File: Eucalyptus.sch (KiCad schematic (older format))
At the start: 39 parts

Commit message: modificaciones
se empezo el sch y pcb
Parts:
- removed C? (x2): 10uF, EESTN5:CAP_ELEC_5x11mm, symbol Eucalyptus-rescue:CAPAPOL-2018---MiniSumo---NANO---DRV8872-rescue
- removed J?: Sensor TATAMI FI, EESTN5:Pin_Strip_3, symbol Eucalyptus-rescue:CONN_01X03-2018---MiniSumo---NANO---DRV8872-rescue
- removed J?: Sensor TATAMI TD, EESTN5:Pin_Strip_3, symbol Eucalyptus-rescue:CONN_01X03-2018---MiniSumo---NANO---DRV8872-rescue
- removed J?: Sensor TATAMI FD, EESTN5:Pin_Strip_3, symbol Eucalyptus-rescue:CONN_01X03-2018---MiniSumo---NANO---DRV8872-rescue
- removed J?: Bateria, EESTN5:BORNERA2_AZUL, symbol Eucalyptus-rescue:TB_1X2-2018---MiniSumo---NANO---DRV8872-rescue
- removed J?: Frontal Izquierdo, EESTN5:Pin_Strip_3, symbol Eucalyptus-rescue:CONN_01X03-2018---MiniSumo---NANO---DRV8872-rescue
- removed J?: Izquierdo, EESTN5:Pin_Strip_3, symbol Eucalyptus-rescue:CONN_01X03-2018---MiniSumo---NANO---DRV8872-rescue
- removed J?: Derecho, EESTN5:Pin_Strip_3, symbol Eucalyptus-rescue:CONN_01X03-2018---MiniSumo---NANO---DRV8872-rescue
- removed J?: Frontal Derecho, EESTN5:Pin_Strip_3, symbol Eucalyptus-rescue:CONN_01X03-2018---MiniSumo---NANO---DRV8872-rescue
- added C12, C14: C, EESTN5:C_1206, symbol EESTN5:C
- added C13, C15: CAPAPOL, EESTN5:CAP_ELEC_SMD_4X5.5, symbol EESTN5:CAPAPOL
- added Display1: SSD1306-SSD1306-128x64_OLED, EESTN5:128x64OLED, symbol EESTN5:SSD1306-SSD1306-128x64_OLED
- added H1, H2, H3, H4: Mounting_Hole, EESTN5:Separador_M3_5mm, symbol EESTN5:Mounting_Hole
- added J1, J16, J17: HEADER_2, Connector_JST:JST_EH_B2B-EH-A_1x02_P2.50mm_Vertical, symbol EESTN5:HEADER_2
- added J11, J12, J13, J14, J15, J3, J4, J5, J6, J7, J8, J9: HEADER_1, EESTN5:PAD_SMD_2x5mm, symbol EESTN5:HEADER_1
- added R10, R9: R, EESTN5:R_1206, symbol EESTN5:R
- added R11, R12: 0,,25, EESTN5:R_1206, symbol EESTN5:R
- added U3, U4: DRV8872, EESTN5:SSOP-8, symbol EESTN5:DRV8872
- C1, C10, C4: renamed from C?; footprint EESTN5:CAP_ELEC_5x11mm -> EESTN5:CAP_ELEC_SMD_4X5.5
- R4, R5: renamed from R?; footprint EESTN5:RES0.3 -> EESTN5:R_1206
- SW1: renamed from SW?; footprint EESTN5:Pulsador_TH_4 -> Button_Switch_SMD:SW_SPST_TL3342
- Y1: renamed from Y?; footprint EESTN5:HC49_SMD -> EESTN5:C_1206
- gave numbers to parts that had none: 22
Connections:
- net +5V: now also Display1.2 (VCC), J11.1, J14.1, J4.1, J7.1, R10.1, R9.1
- net DISTANCIA_D: now also J8.1
- net DISTANCIA_FD: now also J12.1
- net DISTANCIA_FI: now also J15.1
- net DISTANCIA_I: now also J5.1
- net GND: now also C12.2, C13.2, C14.2, C15.2, Display1.1 (GND), J1.1, J13.1, J3.1, J6.1, J9.1, R11.2, R12.2, U3.1 (GND), U4.1 (GND)
- net M1A: now also U3.2 (IN2)
- net M1B: now also U3.3 (IN1)
- net M2A: now also U4.2 (IN2)
- net M2B: now also U4.3 (IN1)
- net Vin: now also C12.1, C13.1, C14.1, C15.1, J1.2, U3.5 (VM), U4.5 (VM)
- net TATAMI_FD renamed SDA
- net SDA: now also Display1.4 (SDA), R10.2
- net TATAMI_FI renamed SCL
- net SCL: now also Display1.3 (SCL), R9.2
- new net: R11.1, U3.7 (ISEN)
- new net: J16.2, U3.6 (OUT1)
- new net: J16.1, U3.8 (OUT2)
- new net: J17.2, U4.6 (OUT1)
- new net: R12.1, U4.7 (ISEN)
- new net: J17.1, U4.8 (OUT2)
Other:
- moved on the sheet: BZ1, C1, C10, C11, C3, C4, C6, C7, C8, C9, D1, D2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

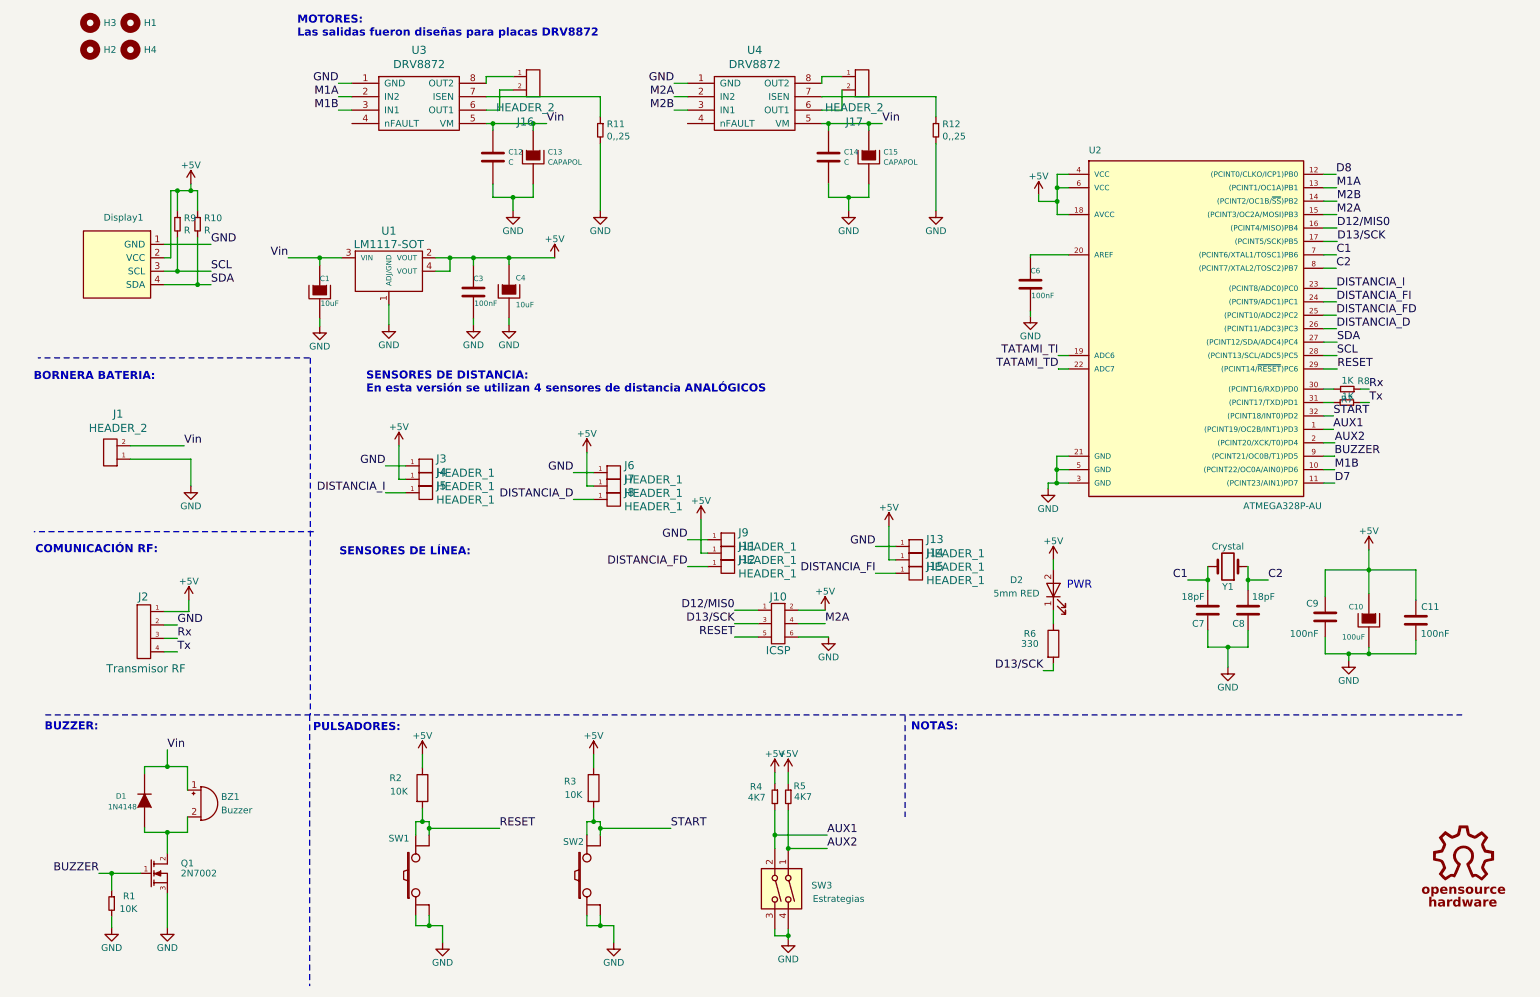
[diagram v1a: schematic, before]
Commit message: modificaciones
se agrego pdf de sch
pdf de lista de componentes y excel
tambien se modifico sch y pcb
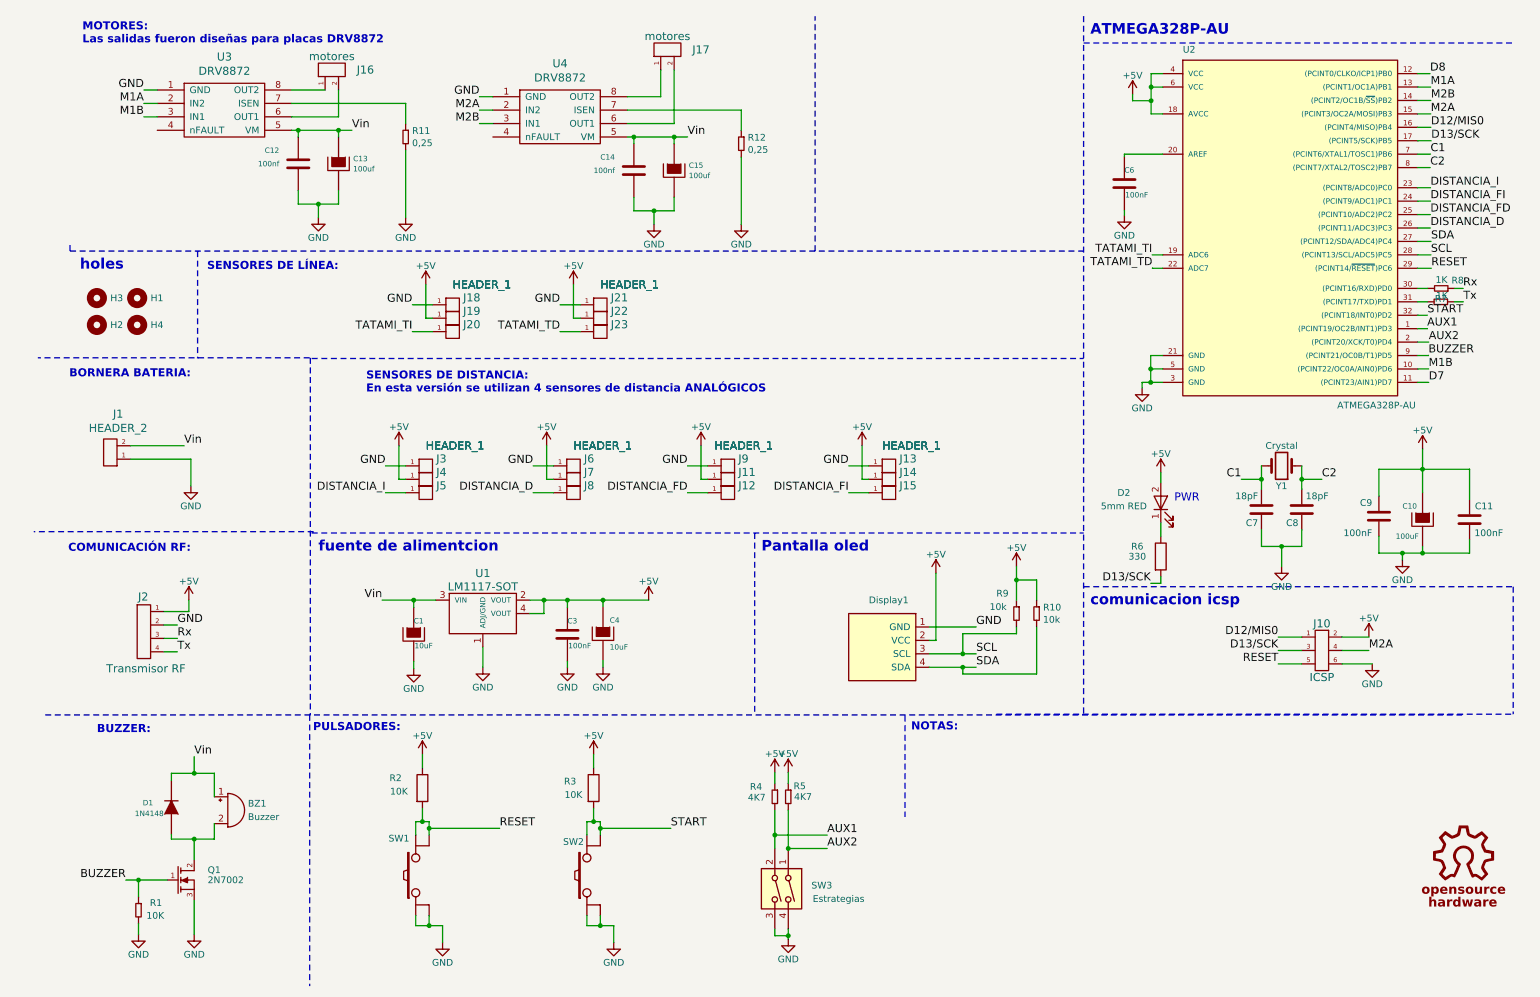
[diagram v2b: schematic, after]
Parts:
- added J18, J19, J20, J21, J22, J23: HEADER_1, EESTN5:PAD_SMD_2x5mm, symbol EESTN5:HEADER_1
- C12, C14: value C -> 100nf
- C13, C15: value CAPAPOL -> 100uf
- J16, J17: value HEADER_2 -> motores
- R10, R9: value R -> 10k
- R11, R12: value 0,,25 -> 0,25
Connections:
- net +5V: now also J19.1, J22.1
- net GND: now also J18.1, J21.1
- net TATAMI_TD: now also J23.1
- net TATAMI_TI: now also J20.1
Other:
- note added: "ATMEGA328P-AU"
- note added: "\nPantalla oled\n"
- note added: "comunicacion icsp"
- note added: "fuente de alimentcion"
- note added: "holes"
- moved on the sheet: BZ1, C1, C10, C11, C12, C13, C14, C15, C3, C4, C6, C7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

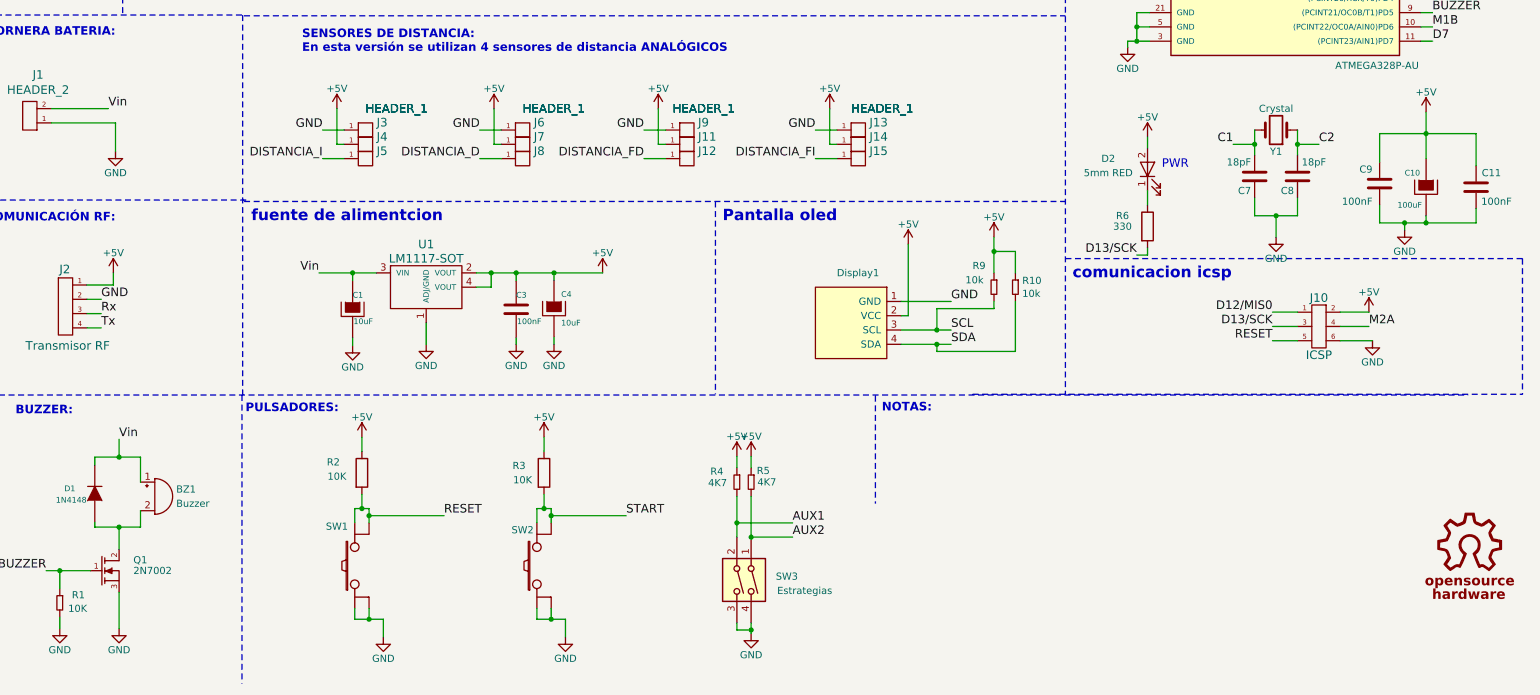
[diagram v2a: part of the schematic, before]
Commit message: modificaciones
se termino el pcb, modifique el cristal en e sch, termine lista de compnentes y genere 2 imagenes de la pcb
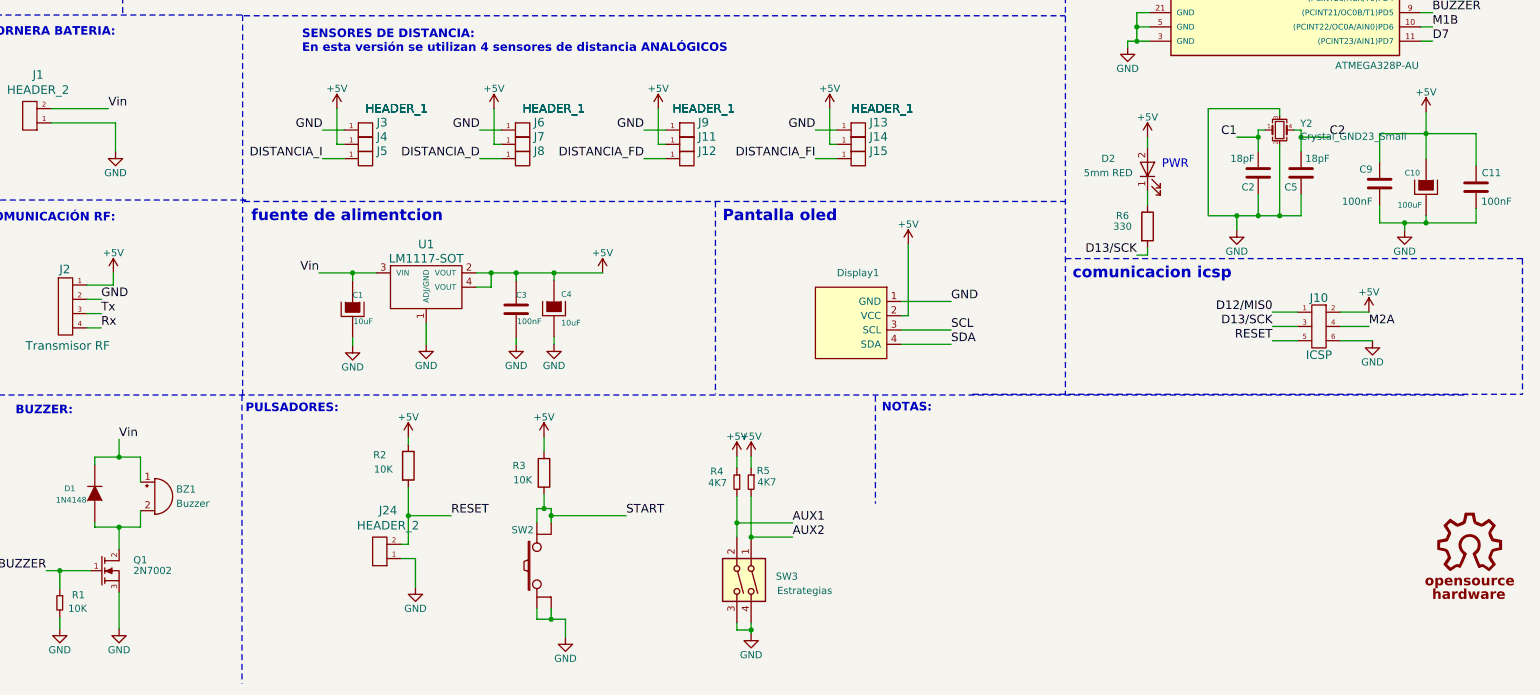
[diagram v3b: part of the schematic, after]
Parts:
- removed C7, C8: 18pF, EESTN5:C_1206, symbol Eucalyptus-rescue:C-2018---MiniSumo---NANO---DRV8872-rescue
- removed R10, R9: 10k, EESTN5:R_1206, symbol EESTN5:R
- removed SW1: SW_PUSH, Button_Switch_SMD:SW_SPST_TL3342, symbol Eucalyptus-rescue:SW_PUSH-2018---MiniSumo---NANO---DRV8872-rescue
- removed Y1: Crystal, EESTN5:C_1206, symbol Eucalyptus-rescue:Crystal-2018---MiniSumo---NANO---DRV8872-rescue
- added C2, C5: 18pF, EESTN5:C_1206, symbol Eucalyptus-rescue:C-2018---MiniSumo---NANO---DRV8872-rescue
- added J24: HEADER_2, EESTN5:SW_SPST_EVQPE1, symbol EESTN5:HEADER_2
- added Y2: Crystal_GND23_Small, Crystal:Crystal_SMD_EuroQuartz_X22-4Pin_2.5x2.0mm, symbol Device:Crystal_GND23_Small
- J11, J12, J13, J14, J15, J18, J19, J20, J21, J22, J23, J3, J4, J5, J6, J7, J8, J9: footprint EESTN5:PAD_SMD_2x5mm -> EESTN5:DUAL_PAD_TH_SMD_2x5mm
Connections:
- net C1: now also C2.2, Y2.1
- net C2: now also C5.2, Y2.4
- net GND: now also C2.1, C5.1, J24.1, Y2.2, Y2.3
- net RESET: now also J24.2
- net Rx: now also J2.4; no longer J2.3
- net Tx: now also J2.3; no longer J2.4

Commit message: MODIFICACIONES
SE MODIFICO PCB,SERIGRAFIA Y ARCHIVOS GERBERS
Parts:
- Display1: footprint EESTN5:128x64OLED -> Eucalyptus:128x64OLED
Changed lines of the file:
@@
 F 0 "Display1" V 6150 5100 50  0000 L CNN
 F 1 "SSD1306-SSD1306-128x64_OLED" H 6500 5150 50  0001 C CNN
-F 2 "EESTN5:128x64OLED" H 6500 5450 50  0001 C CNN
+F 2 "Eucalyptus:128x64OLED" H 6500 5450 50  0001 C CNN
 F 3 "" H 6500 5450 50  0001 C CNN
 	1    6500 5200
